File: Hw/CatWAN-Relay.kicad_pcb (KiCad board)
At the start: 2 copper layers, 53 parts, among them J10 USB_B, J2 INPUTS, J3 OUTPUTS, J4 SWD, J5 Serial, Q1 MMBT2222A, Q2 MMBT2222A, Q3 MMBT2222A, U2 RFM95W-915-868, U3 LTV-817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

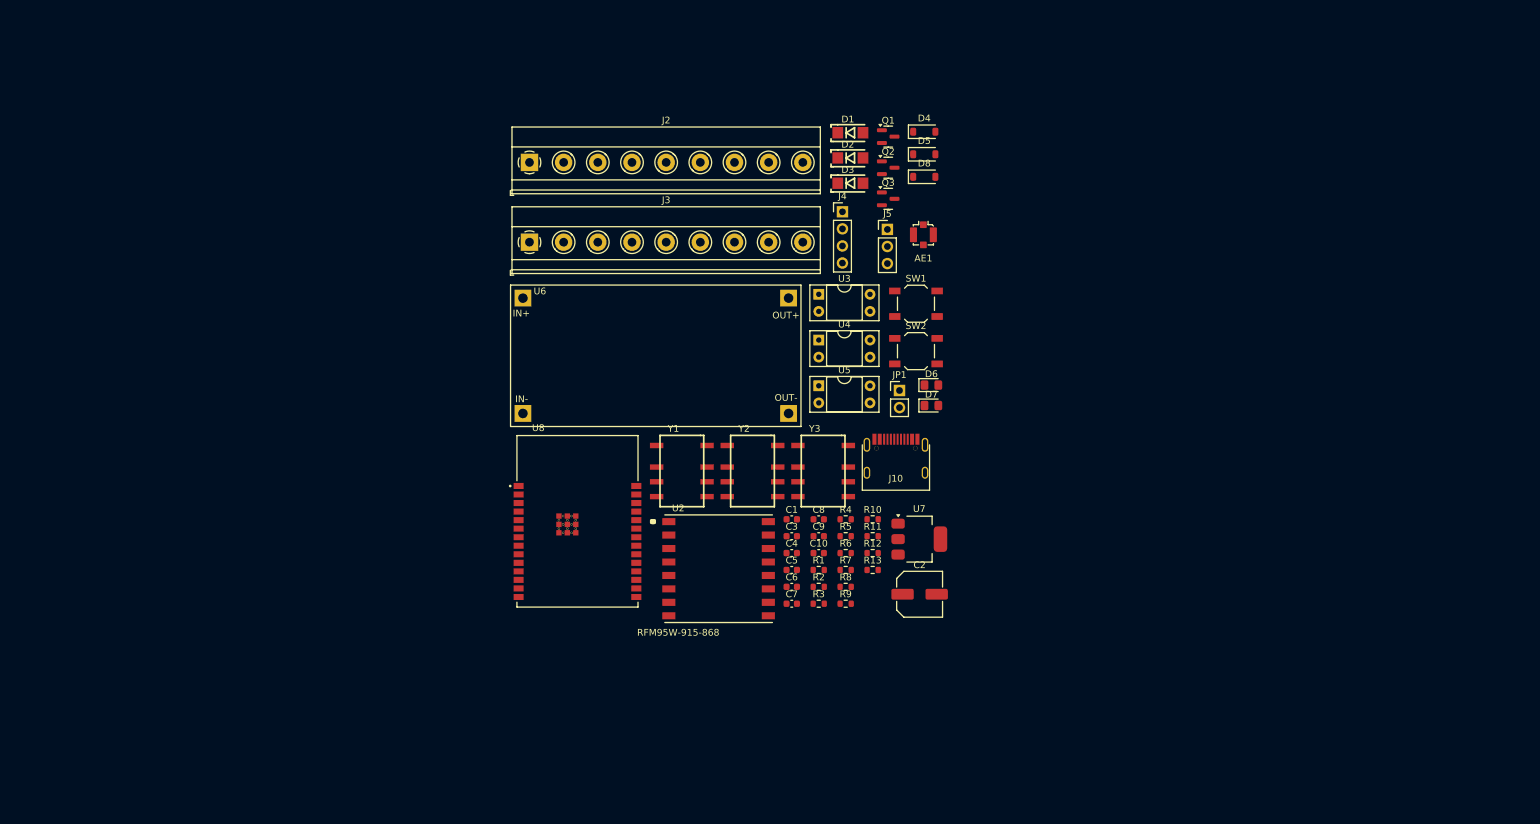
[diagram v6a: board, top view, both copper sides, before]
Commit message: feat: UPDATE BOM & diode changed
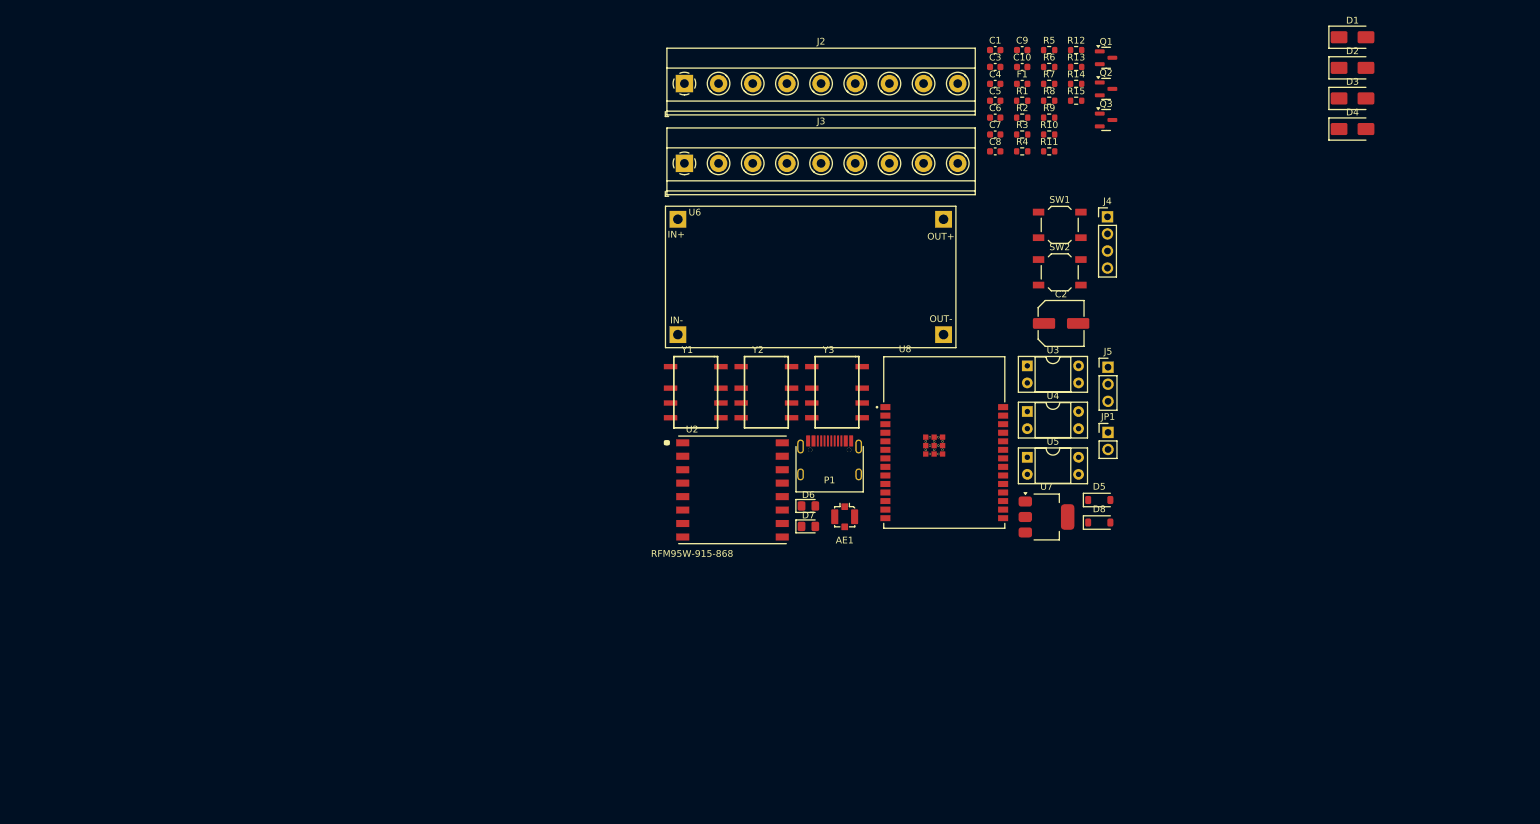
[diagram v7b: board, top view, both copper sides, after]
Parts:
- removed J10: USB_B, agroin:C393939
- added F1: 1A, Fuse:Fuse_0603_1608Metric, F.Cu at (187.9, 43.8)
- added P1: USB_C_Plug_USB2.0, agroin:C393939, F.Cu at (159.3, 97.7)
- added R14: 5.1k, Resistor_SMD:R_0603_1608Metric, F.Cu at (195.9, 43.8)
- added R15: 5.1k, Resistor_SMD:R_0603_1608Metric, F.Cu at (195.9, 46.3)
- D1, D2, D3: value FM4007W-W -> RS1M; footprint agroin:F4007 -> Diode_SMD:D_SMA
- D4: value FM4007W-W -> RS1M; footprint Diode_SMD:D_SOD-123 -> Diode_SMD:D_SMA
- J4: value SWD -> I2C
- SW1: value ~ -> BOOT
- SW2: value ~ -> RESET
- moved R12 80.7 mm to (195.9, 38.8)
- moved R13 80.7 mm to (195.9, 41.3)
- moved C10 78.3 mm to (187.9, 41.3)
- moved C9 78.3 mm to (187.9, 38.8)
- moved R5 78.3 mm to (191.9, 38.8)
- moved R6 78.3 mm to (191.9, 41.3)
- moved R8 78.3 mm to (191.9, 46.3)
- moved R7 78.3 mm to (191.9, 43.8)
- moved R9 78.3 mm to (191.9, 48.8)
- moved D1 77.8 mm to (237.0, 36.9)
- moved D2 77.7 mm to (237.0, 41.4)
- moved D3 77.6 mm to (237.0, 46.0)
- moved C4 76.0 mm to (183.9, 43.8)
- moved C6 76.0 mm to (183.9, 48.8)
- moved R2 76.0 mm to (187.9, 48.8)
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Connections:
- C10 pad 1: /VOUT -> +3V3
- C8 pad 1: /VOUT -> +3V3
- C9 pad 1: /VOUT -> +3V3
- J5 pad 1: /Tx -> /TX
- J5 pad 2: /Rx -> /RX
- R12 pad 2: /VOUT -> +3V3
- R13 pad 2: /VOUT -> +3V3
- U8 pad 2: /VOUT -> +3V3

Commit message: feat(hw): Footprint added
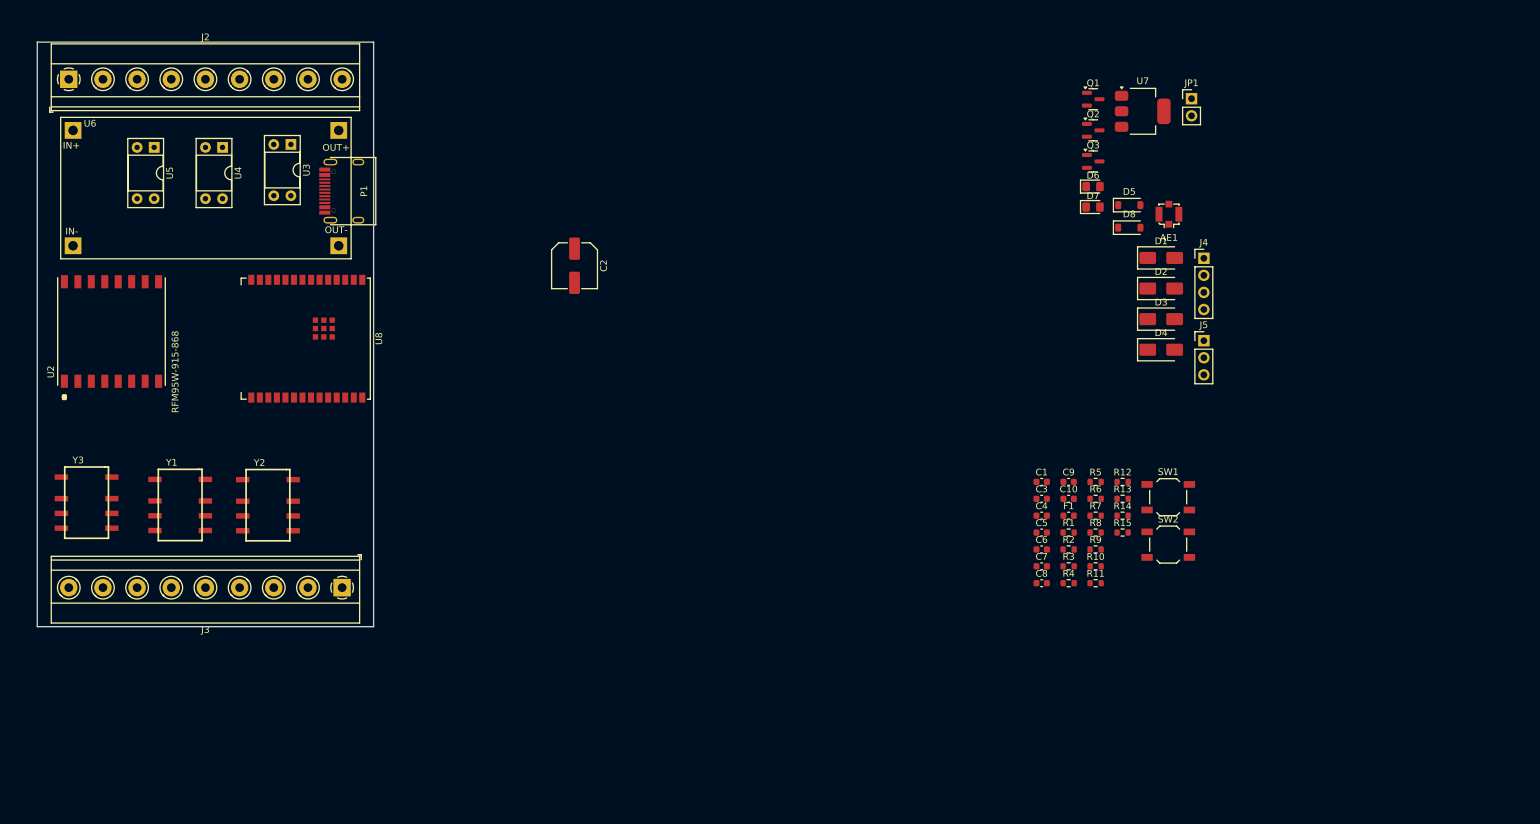
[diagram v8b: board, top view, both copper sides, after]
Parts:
- U8: footprint agroin:XCVR_ESP32-C6-WROOM-1-N8 -> PCM_Espressif:ESP32-C6-WROOM-1U
- moved U5 137.7 mm to (58.9, 53.2), turned to -90 degrees
- moved U4 125.9 mm to (69.0, 53.2), turned to -90 degrees
- moved U3 114.3 mm to (79.2, 52.8), turned to -90 degrees
- moved Y3 112.8 mm to (45.5, 100.7)
- moved U8 96.0 mm to (81.5, 81.7), turned to -90 degrees
- moved U2 95.3 mm to (52.5, 80.6), turned to 90 degrees
- moved J2 91.5 mm to (46.1, 43.1)
- moved U6 90.9 mm to (44.9, 48.8)
- moved P1 83.4 mm to (85.0, 59.7), turned to 90 degrees
- moved J3 81.0 mm to (86.8, 118.7), turned to 180 degrees
- moved Y1 78.5 mm to (59.5, 101.1)
- moved Y2 76.0 mm to (72.5, 101.1)
- moved C2 72.8 mm to (121.3, 70.8), turned to -90 degrees
- moved AE1 65.9 mm to (209.7, 63.2)
- moved C4 64.6 mm to (190.8, 108.0)
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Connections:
- R11 pad 1: /Rx_LED -> /RX_LED
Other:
- board outline added: 50 x 86.9 mm
